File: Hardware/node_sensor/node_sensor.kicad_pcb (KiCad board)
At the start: 2 copper layers, 50 x 50 mm, 14 parts, among them J1 Conn_Jack-DC, J2 Pump, J3 Light, U1 DevKitESP32, U2 DHT11, U3 BH1750, U4 ADS1115, U5 DS3231, U6 Soil-Moisture, U7 Soil-Moisture, U8 Soil-Moisture, U9 Soil-Moisture

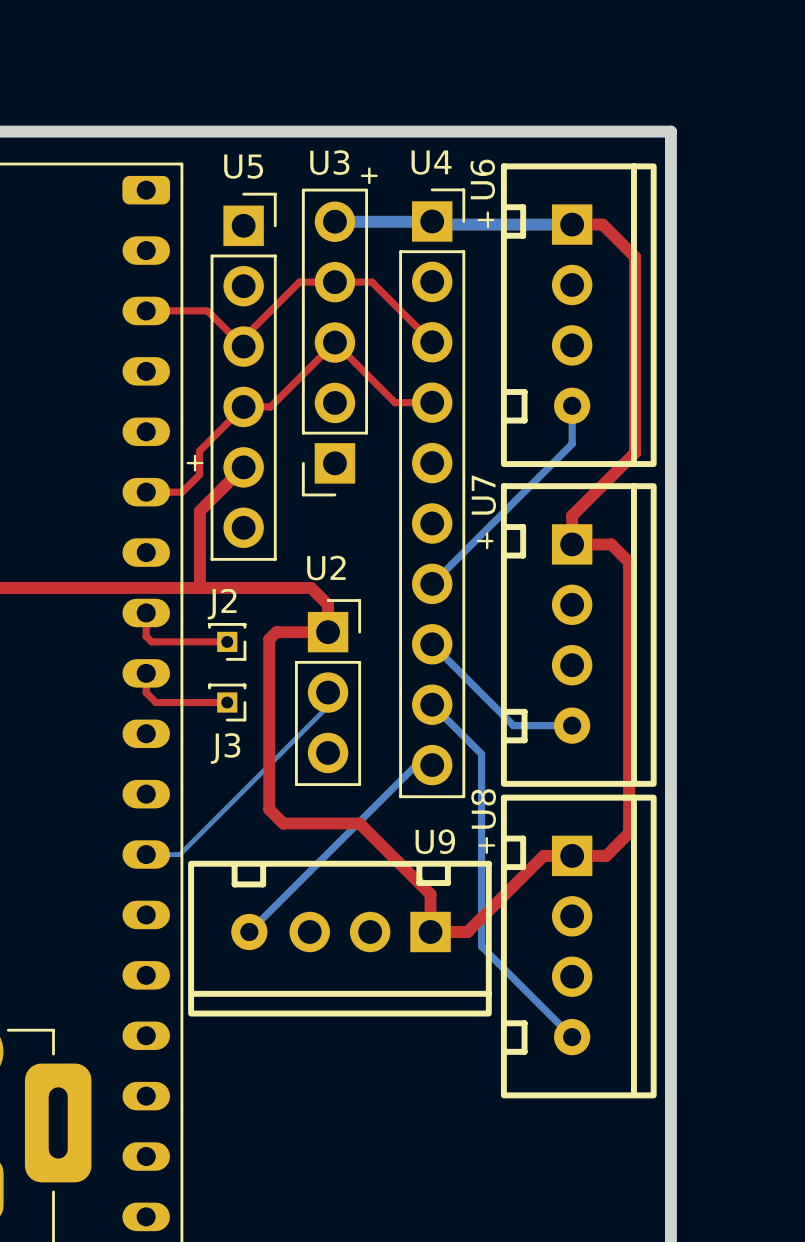
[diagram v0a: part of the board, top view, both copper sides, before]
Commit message: "updated topic DT in Unity"
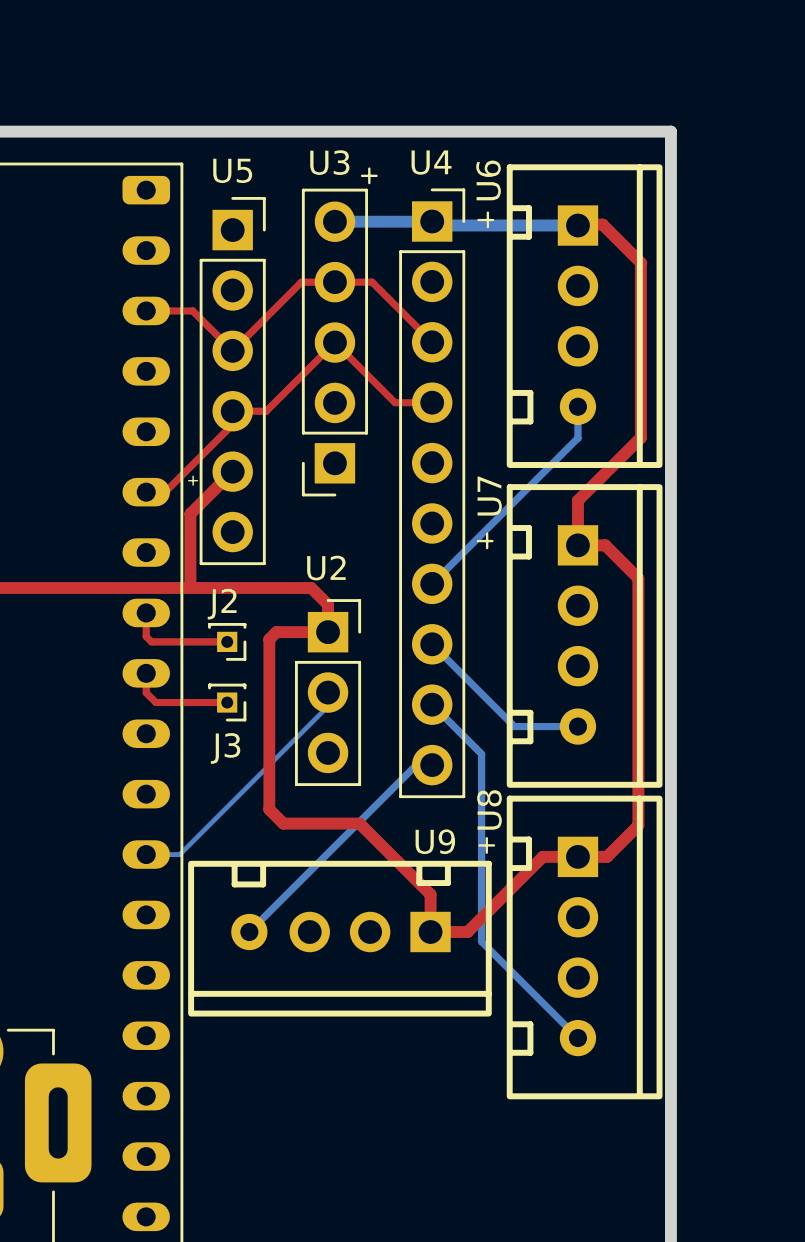
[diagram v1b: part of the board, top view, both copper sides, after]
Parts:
- moved U5 0.49 mm to (121.6, 44.1)
- moved U8 0.25 mm to (136.1, 74.3)
- moved U6 0.25 mm to (136.1, 47.8)
- moved U7 0.25 mm to (136.1, 61.2)
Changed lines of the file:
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@@
 		(capping no)
 		(filling no)
-		(zone_defaults)
 		(pcbplotparams
 			(layerselection 0x00000000_00000000_55555555_5755f5ff)
@@
 	(footprint "MY_FOOTPRINTS:Conn_XH-P2.54mm-4P"
 		(layer "F.Cu")
-		(at 135.845 47.72)
+		(at 136.09 47.76)
 		(tags "XH 2.54 ")
 		(property "Reference" "U6"
@@
 	(footprint "Connector_PinSocket_2.54mm:PinSocket_1x06_P2.54mm_Vertical"
 		(layer "F.Cu")
-		(at 122.03 43.96)
+		(at 121.57 44.14)
 		(descr "Through hole straight socket strip, 1x06, 2.54mm pitch, single row (from Kicad 4.0.7), script generated")
 		(tags "Through hole socket strip THT 1x06 2.54mm single row")
@@
 		(sheetname "/")
 		(sheetfile "node_sensor.kicad_sch")
-		(units
-			(unit
-				(name "A")
-				(pins "1" "2" "3" "4" "5" "6")
-			)
-		)
 		(attr through_hole)
 		(duplicate_pad_numbers_are_jumpers no)
@@
 	(footprint "MY_FOOTPRINTS:Conn_XH-P2.54mm-4P"
 		(layer "F.Cu")
-		(at 135.845 74.27)
+		(at 136.09 74.31)
 		(tags "XH 2.54 ")
 		(property "Reference" "U8"
@@
 	(footprint "MY_FOOTPRINTS:Conn_XH-P2.54mm-4P"
 		(layer "F.Cu")
-		(at 135.845 61.17)
+		(at 136.09 61.21)
 		(tags "XH 2.54 ")
 		(property "Reference" "U7"
@@
 	)
 	(gr_line
-		(start 119.68 53.94)
-		(end 120.29 53.94)
+		(start 119.720572 54.68)
+		(end 120.09 54.68)
 		(stroke
-			(width 0.1)
+			(width 0.060563)
 			(type default)
 		)
@@
 	)
 	(gr_line
-		(start 119.985 53.635)
-		(end 119.985 54.245)
+		(start 119.905286 54.495286)
+		(end 119.905286 54.864714)
 		(stroke
-			(width 0.1)
+			(width 0.060563)
 			(type default)
 		)
@@
 	)
 	(segment
-		(start 129.89 73.66)
-		(end 131.45 73.66)
+		(start 136.09 70.5)
+		(end 137.31 70.5)
 		(width 0.5)
 		(layer "F.Cu")
@@
 	)
 	(segment
-		(start 125.58 59.9)
-		(end 125.58 61.05)
+		(start 119.79 59.18272)
+		(end 119.79 56.08)
 		(width 0.5)
 		(layer "F.Cu")
@@
 	)
 	(segment
-		(start 137.28 70.46)
-		(end 135.845 70.46)
+		(start 138.63 69.18)
+		(end 138.63 58.79)
 		(width 0.5)
 		(layer "F.Cu")
@@
 	)
 	(segment
-		(start 123.11 61.35)
-		(end 123.11 68.51)
+		(start 125.58 59.9)
+		(end 125.58 61.05)
 		(width 0.5)
 		(layer "F.Cu")
@@
 	)
 	(segment
-		(start 138.24 69.5)
-		(end 137.28 70.46)
+		(start 134.61 70.5)
+		(end 136.09 70.5)
 		(width 0.5)
 		(layer "F.Cu")
@@
 	)
 	(segment
-		(start 138.24 58.11)
-		(end 138.24 69.5)
+		(start 123.11 61.35)
+		(end 123.11 68.51)
 		(width 0.5)
 		(layer "F.Cu")
@@
 	)
 	(segment
-		(start 123.41 61.05)
-		(end 123.11 61.35)
+		(start 135.845 43.91)
+		(end 135.715 43.78)
 		(width 0.5)
 		(layer "F.Cu")
@@
 	)
 	(segment
-		(start 109.26368 59.19272)
-		(end 120.19 59.19272)
+		(start 123.41 61.05)
+		(end 123.11 61.35)
 		(width 0.5)
 		(layer "F.Cu")
@@
 	)
 	(segment
-		(start 92.53368 42.46272)
-		(end 109.26368 59.19272)
+		(start 136.09 57.4)
+		(end 136.09 55.52)
 		(width 0.5)
 		(layer "F.Cu")
@@
 	)
 	(segment
-		(start 120.19 55.96)
-		(end 120.19 59.19272)
+		(start 131.45 73.66)
+		(end 134.61 70.5)
 		(width 0.5)
 		(layer "F.Cu")
@@
 	)
 	(segment
-		(start 137.49 57.36)
-		(end 138.24 58.11)
-		(width 0.5)
-		(layer "F.Cu")
-		(net "+3V3")
-	)
-	(segment
-		(start 138.49 45.27)
-		(end 137.13 43.91)
+		(start 137.31 70.5)
+		(end 138.63 69.18)
 		(width 0.5)
 		(layer "F.Cu")
@@
 	)
 	(segment
-		(start 135.845 56.155)
-		(end 138.49 53.51)
+		(start 92.53368 42.46272)
+		(end 109.26368 59.19272)
 		(width 0.5)
 		(layer "F.Cu")
@@
 	)
 	(segment
-		(start 122.03 54.12)
-		(end 120.19 55.96)
+		(start 129.89 73.66)
+		(end 131.45 73.66)
 		(width 0.5)
 		(layer "F.Cu")
@@
 	)
 	(segment
-		(start 138.49 53.51)
-		(end 138.49 45.27)
+		(start 123.7 69.1)
+		(end 126.91 69.1)
 		(width 0.5)
 		(layer "F.Cu")
@@
 	)
 	(segment
-		(start 123.7 69.1)
-		(end 126.91 69.1)
+		(start 126.91 69.1)
+		(end 129.89 72.08)
 		(width 0.5)
 		(layer "F.Cu")
@@
 	)
 	(segment
-		(start 126.91 69.1)
-		(end 129.89 72.08)
+		(start 123.11 68.51)
+		(end 123.7 69.1)
 		(width 0.5)
 		(layer "F.Cu")
@@
 	)
 	(segment
-		(start 131.45 73.66)
-		(end 134.65 70.46)
+		(start 109.26368 59.19272)
+		(end 120.19 59.19272)
 		(width 0.5)
 		(layer "F.Cu")
@@
 	)
 	(segment
-		(start 123.11 68.51)
-		(end 123.7 69.1)
+		(start 138.735 45.515)
+		(end 137.13 43.91)
 		(width 0.5)
 		(layer "F.Cu")
@@
 	)
 	(segment
-		(start 135.845 57.36)
-		(end 137.49 57.36)
+		(start 119.79 56.08)
+		(end 121.57 54.3)
 		(width 0.5)
 		(layer "F.Cu")
@@
 	)
 	(segment
-		(start 137.13 43.91)
-		(end 135.845 43.91)
+		(start 119.8 59.19272)
+		(end 119.79 59.18272)
 		(width 0.5)
 		(layer "F.Cu")
@@
 	)
 	(segment
-		(start 135.715 43.78)
+		(start 137.13 43.91)
 		(end 135.845 43.91)
 		(width 0.5)
@@
 	)
 	(segment
-		(start 135.845 57.36)
-		(end 135.845 56.155)
+		(start 138.63 58.79)
+		(end 137.24 57.4)
 		(width 0.5)
 		(layer "F.Cu")
@@
 	)
 	(segment
-		(start 134.65 70.46)
-		(end 135.845 70.46)
+		(start 138.735 52.875)
+		(end 138.735 45.515)
+		(width 0.5)
+		(layer "F.Cu")
+		(net "+3V3")
+	)
+	(segment
+		(start 136.09 55.52)
+		(end 138.735 52.875)
 		(width 0.5)
 		(layer "F.Cu")
@@
 	)
 	(segment
-		(start 130.09 43.91)
+		(start 137.24 57.4)
+		(end 136.09 57.4)
+		(width 0.5)
+		(layer "F.Cu")
+		(net "+3V3")
+	)
+	(segment
+		(start 130.13 43.95)
 		(end 129.96 43.78)
 		(width 0.5)
@@
 	)
 	(segment
-		(start 135.845 43.91)
-		(end 130.09 43.91)
+		(start 136.09 43.95)
+		(end 130.13 43.95)
 		(width 0.5)
 		(layer "B.Cu")
@@
 	)
 	(segment
-		(start 135.845 53.135)
-		(end 129.96 59.02)
+		(start 136.09 51.57)
+		(end 136.09 52.89)
 		(width 0.3)
 		(layer "B.Cu")
@@
 	)
 	(segment
-		(start 135.845 51.53)
-		(end 135.845 53.135)
+		(start 136.09 52.89)
+		(end 129.96 59.02)
 		(width 0.3)
 		(layer "B.Cu")
@@
 	)
 	(segment
-		(start 120.18 54.43)
-		(end 120.18 53.43)
+		(start 118.72728 55.16272)
+		(end 117.93368 55.16272)
 		(width 0.3)
 		(layer "F.Cu")
@@
 	)
 	(segment
-		(start 120.18 53.43)
-		(end 122.03 51.58)
-		(width 0.3)
-		(layer "F.Cu")
-		(net "/I2C_SDA")
-	)
-	(segment
-		(start 117.93368 55.16272)
-		(end 119.44728 55.16272)
+		(start 121.57 51.76)
+		(end 121.57 52.32)
 		(width 0.3)
 		(layer "F.Cu")
@@
 	(segment
 		(start 125.87 48.87)
-		(end 128.4 51.4)
+		(end 122.98 51.76)
 		(width 0.3)
 		(layer "F.Cu")
@@
 	)
 	(segment
-		(start 123.16 51.58)
-		(end 122.03 51.58)
+		(start 121.57 52.32)
+		(end 118.72728 55.16272)
 		(width 0.3)
 		(layer "F.Cu")
@@
 	(segment
 		(start 125.87 48.87)
-		(end 123.16 51.58)
+		(end 128.4 51.4)
 		(width 0.3)
 		(layer "F.Cu")
@@
 	)
 	(segment
-		(start 119.44728 55.16272)
-		(end 120.18 54.43)
+		(start 122.98 51.76)
+		(end 121.57 51.76)
 		(width 0.3)
 		(layer "F.Cu")
@@
 	)
 	(segment
-		(start 124.38 46.33)
-		(end 121.84 48.87)
+		(start 124.46 46.33)
+		(end 121.57 49.22)
 		(width 0.3)
 		(layer "F.Cu")
@@
 	)
 	(segment
-		(start 121.84 48.87)
-		(end 120.51272 47.54272)
+		(start 125.87 46.33)
+		(end 124.46 46.33)
 		(width 0.3)
 		(layer "F.Cu")
@@
 	)
 	(segment
-		(start 120.51272 47.54272)
-		(end 117.93368 47.54272)
+		(start 121.57 49.22)
+		(end 119.89272 47.54272)
 		(width 0.3)
 		(layer "F.Cu")
@@
 	)
 	(segment
-		(start 125.87 46.33)
-		(end 124.38 46.33)
+		(start 119.89272 47.54272)
+		(end 117.93368 47.54272)
 		(width 0.3)
 		(layer "F.Cu")
@@
 	)
 	(segment
-		(start 133.38 64.98)
+		(start 133.42 65.02)
 		(end 129.96 61.56)
 		(width 0.3)
@@
 	)
 	(segment
-		(start 135.845 64.98)
-		(end 133.38 64.98)
+		(start 136.09 65.02)
+		(end 133.42 65.02)
 		(width 0.3)
 		(layer "B.Cu")
@@
 	)
 	(segment
-		(start 132.04 74.275)
-		(end 135.845 78.08)
+		(start 132.04 74.07)
+		(end 136.09 78.12)
 		(width 0.3)
 		(layer "B.Cu")
@@
 	)
 	(segment
-		(start 132.04 66.18)
-		(end 132.04 74.275)
+		(start 129.96 64.1)
+		(end 132.04 66.18)
 		(width 0.3)
 		(layer "B.Cu")
@@
 	)
 	(segment
-		(start 129.96 64.1)
-		(end 132.04 66.18)
+		(start 132.04 66.18)
+		(end 132.04 74.07)
 		(width 0.3)
 		(layer "B.Cu")
